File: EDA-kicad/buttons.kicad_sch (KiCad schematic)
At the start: 4 parts, among them SW4 PROG, SW5 VOL-, SW6 VOL+, SW7 POW

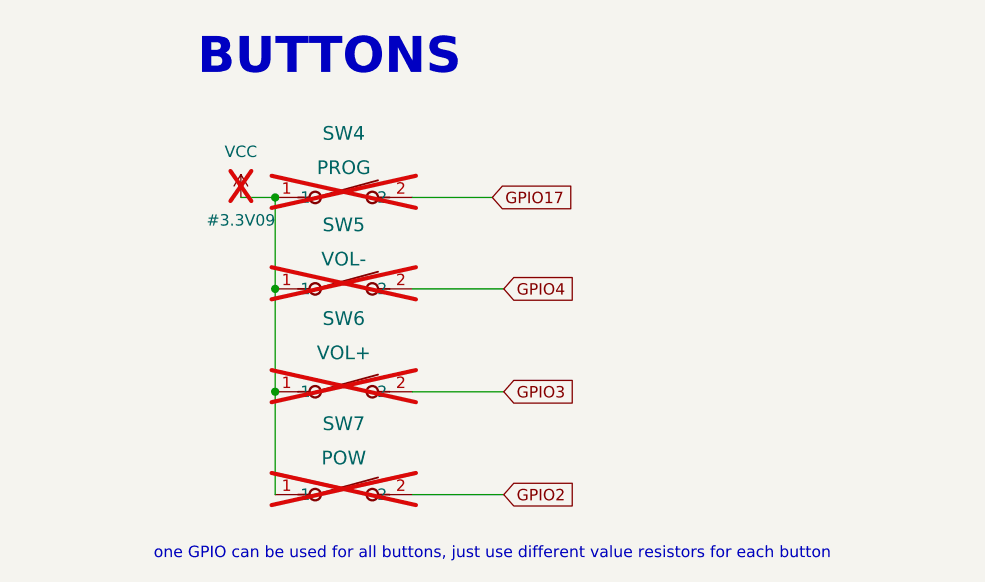
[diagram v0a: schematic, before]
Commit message: reannotate entire schematic
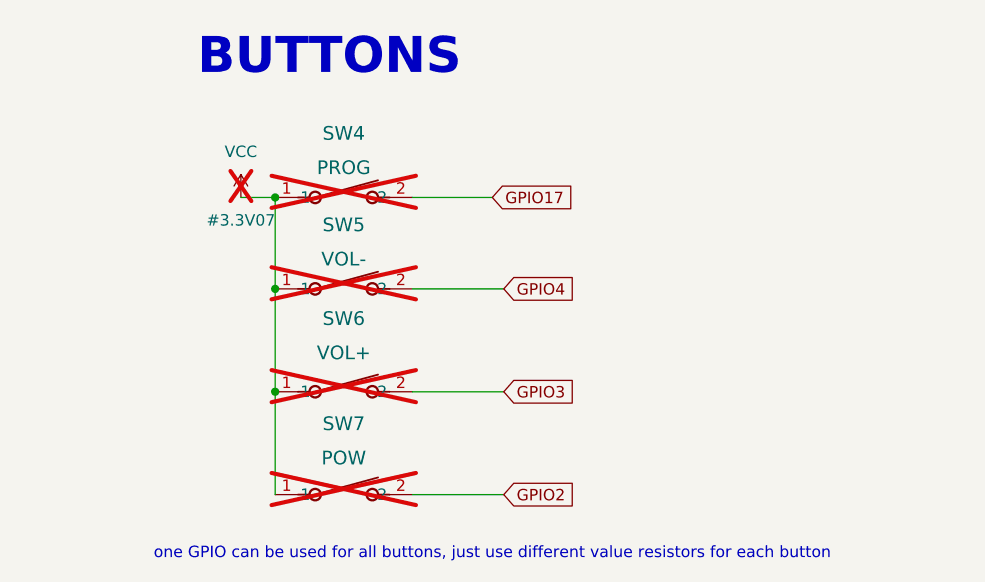
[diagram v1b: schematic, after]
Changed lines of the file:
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@@
 		(on_board yes)
 		(dnp yes)
-		(property "Reference" "#3.3V09"
+		(property "Reference" "#3.3V07"
 			(at 119.38 77.47 0)
 			(effects
@@
 			(project "cm5-carrier"
 				(path "/28c5e4fe-1ec7-4477-97f0-d2ec1401fad5/7d72c53e-b066-4e49-bdb9-37372138f009"
-					(reference "#3.3V09")
+					(reference "#3.3V07")
 					(unit 1)
 				)
